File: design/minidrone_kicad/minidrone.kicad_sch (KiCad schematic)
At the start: 34 parts, among them J1 programming, J2 HM-13 Bluetooth, J3 BAT, J4 mpu6050, J5 FL Motor, J6 BL Motor, J7 FR Motor, J8 BR Motor, Q1 SI2302, Q2 SI2302, Q3 SI2302, Q4 SI2302, U1 stm32_BluePill

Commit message: fix(PCH/PCB): Programming pins and motor pins definition.
Correct the programming TX/RX connection.
Update the motor net-names due to the design changed.
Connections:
- net BL_PWM: now also Q3.1, R10.1, U1.32 (PA7); no longer Q2.1, R9.1, U1.31 (PA6)
- net BR_PWM: now also Q1.1, R8.1, U1.33 (PB0); no longer Q4.1, R11.1, U1.34 (PB1)
- net FL_PWM: now also Q4.1, R11.1, U1.34 (PB1); no longer Q1.1, R8.1, U1.33 (PB0)
- net FR_PWM: now also Q2.1, R9.1, U1.31 (PA6); no longer Q3.1, R10.1, U1.32 (PA7)
- net PRG_RX: now also J1.3 (Pin_3); no longer J1.4 (Pin_4)
- net PRG_TX: now also J1.4 (Pin_4); no longer J1.3 (Pin_3)
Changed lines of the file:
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@@
+		)
+	)
+	(label "FR_PWM"
+		(at 90.17 99.06 0)
+		(fields_autoplaced yes)
+		(effects
+			(font
+				(size 1.27 1.27)
+			)
+			(justify left bottom)
 		)
 	)
@@
 		)
 	)
-	(label "BR_PWM"
-		(at 90.17 91.44 0)
-		(fields_autoplaced yes)
-		(effects
-			(font
-				(size 1.27 1.27)
-			)
-			(justify left bottom)
-		)
-	)
-	(label "FL_PWM"
-		(at 140.97 99.06 0)
-		(fields_autoplaced yes)
-		(effects
-			(font
-				(size 1.27 1.27)
-			)
-			(justify left bottom)
-		)
-	)
 	(label "PRG_RX"
 		(at 41.91 96.52 0)
@@
 		)
 	)
-	(label "BL_PWM"
-		(at 140.97 142.24 0)
-		(fields_autoplaced yes)
-		(effects
-			(font
-				(size 1.27 1.27)
-			)
-			(justify left bottom)
-		)
-	)
 	(label "STAT_3"
 		(at 90.17 106.68 0)
@@
 		)
 	)
+	(label "PRG_TX"
+		(at 27.94 30.48 0)
+		(fields_autoplaced yes)
+		(effects
+			(font
+				(size 1.27 1.27)
+			)
+			(justify left bottom)
+		)
+	)
 	(label "MPU_SCL"
 		(at 40.64 116.84 0)
@@
 		)
 	)
-	(label "FR_PWM"
-		(at 90.17 96.52 0)
+	(label "BR_PWM"
+		(at 140.97 99.06 0)
 		(fields_autoplaced yes)
 		(effects
@@
 		)
 	)
+	(label "BR_PWM"
+		(at 90.17 93.98 0)
+		(fields_autoplaced yes)
+		(effects
+			(font
+				(size 1.27 1.27)
+			)
+			(justify left bottom)
+		)
+	)
 	(label "STAT_0"
 		(at 237.49 22.86 0)
@@
 		)
 	)
-	(label "FL_PWM"
-		(at 90.17 93.98 0)
-		(fields_autoplaced yes)
-		(effects
-			(font
-				(size 1.27 1.27)
-			)
-			(justify left bottom)
-		)
-	)
 	(label "BT_TX"
 		(at 90.17 86.36 0)
@@
 		)
 	)
+	(label "PRG_RX"
+		(at 27.94 27.94 0)
+		(fields_autoplaced yes)
+		(effects
+			(font
+				(size 1.27 1.27)
+			)
+			(justify left bottom)
+		)
+	)
+	(label "FL_PWM"
+		(at 90.17 91.44 0)
+		(fields_autoplaced yes)
+		(effects
+			(font
+				(size 1.27 1.27)
+			)
+			(justify left bottom)
+		)
+	)
 	(label "VBAT"
 		(at 161.29 33.02 0)
@@
 		)
 	)
-	(label "PRG_RX"
-		(at 27.94 30.48 0)
+	(label "BL_PWM"
+		(at 184.15 99.06 0)
 		(fields_autoplaced yes)
 		(effects
@@
 		)
 	)
+	(label "BL_PWM"
+		(at 90.17 96.52 0)
+		(fields_autoplaced yes)
+		(effects
+			(font
+				(size 1.27 1.27)
+			)
+			(justify left bottom)
+		)
+	)
 	(label "MPU_SCL"
 		(at 187.96 36.83 0)
@@
 		)
 	)
-	(label "BL_PWM"
-		(at 90.17 99.06 0)
-		(fields_autoplaced yes)
-		(effects
-			(font
-				(size 1.27 1.27)
-			)
-			(justify left bottom)
-		)
-	)
 	(label "BT_RX"
 		(at 90.17 88.9 0)
@@
 		)
 	)
+	(label "FR_PWM"
+		(at 140.97 142.24 0)
+		(fields_autoplaced yes)
+		(effects
+			(font
+				(size 1.27 1.27)
+			)
+			(justify left bottom)
+		)
+	)
 	(label "PRG_TX"
 		(at 41.91 99.06 0)
@@
 		)
 	)
-	(label "PRG_TX"
-		(at 27.94 27.94 0)
-		(fields_autoplaced yes)
-		(effects
-			(font
-				(size 1.27 1.27)
-			)
-			(justify left bottom)
-		)
-	)
-	(label "FR_PWM"
-		(at 184.15 99.06 0)
+	(label "FL_PWM"
+		(at 184.15 142.24 0)
 		(fields_autoplaced yes)
 		(effects
@@
 		(fields_autoplaced yes)
 		(effects
-			(font
-				(size 1.27 1.27)
-			)
-			(justify left bottom)
-		)
-	)
-	(label "BR_PWM"
-		(at 184.15 142.24 0)
-		(fields_autoplaced yes)
-		(effects

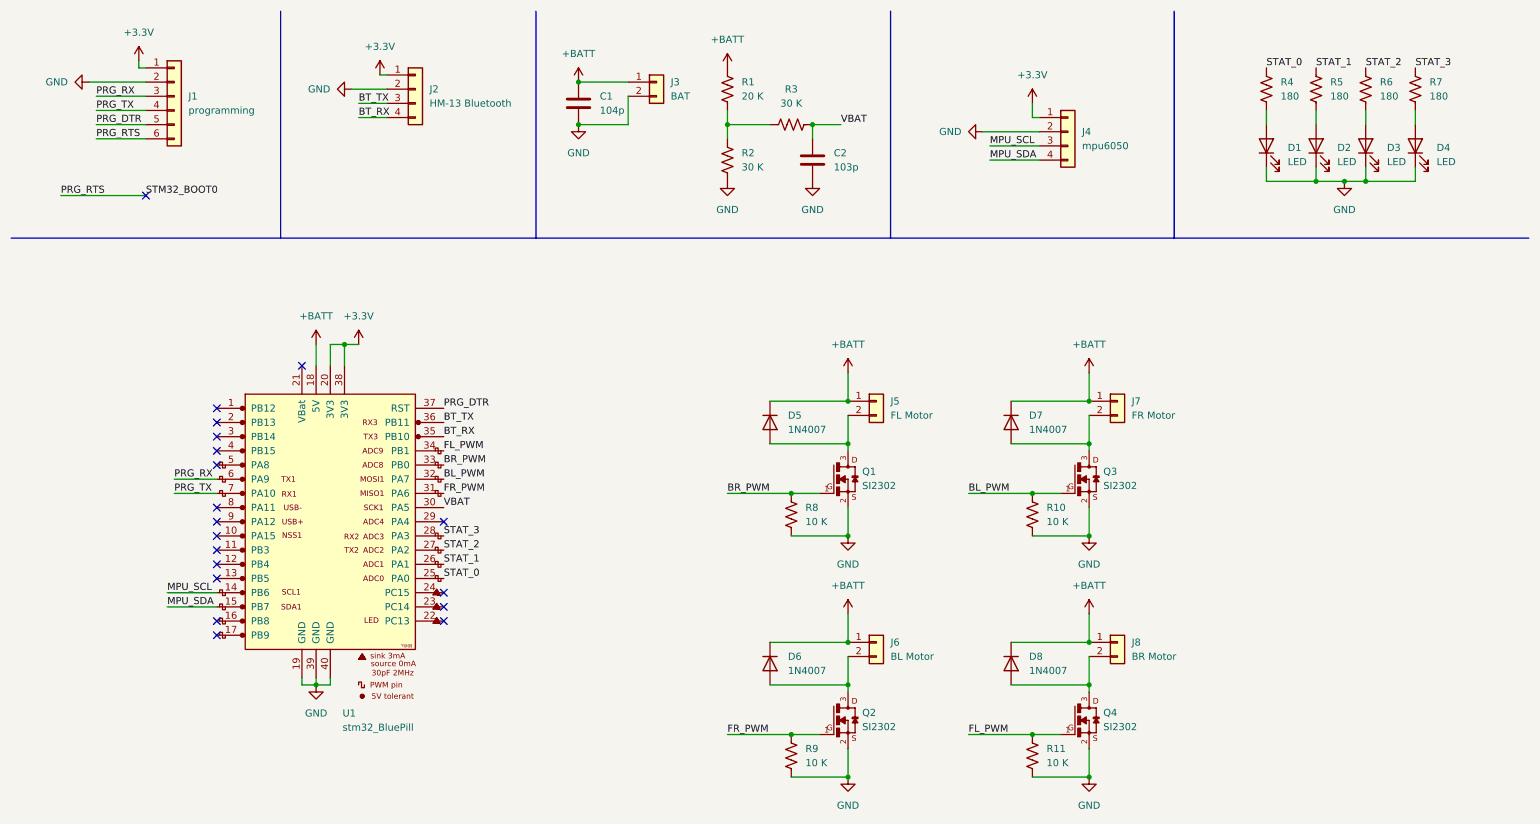
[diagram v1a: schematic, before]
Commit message: docs(SCH/PCB): Update the PCB design to v2.
The v1's handmade version is too heavy.
 - Remove the STM32 blue pill board.
 - Using the STM32F103CBT6 to make sure the ROM size enough.
 - Design the PCB as the drone's frame.
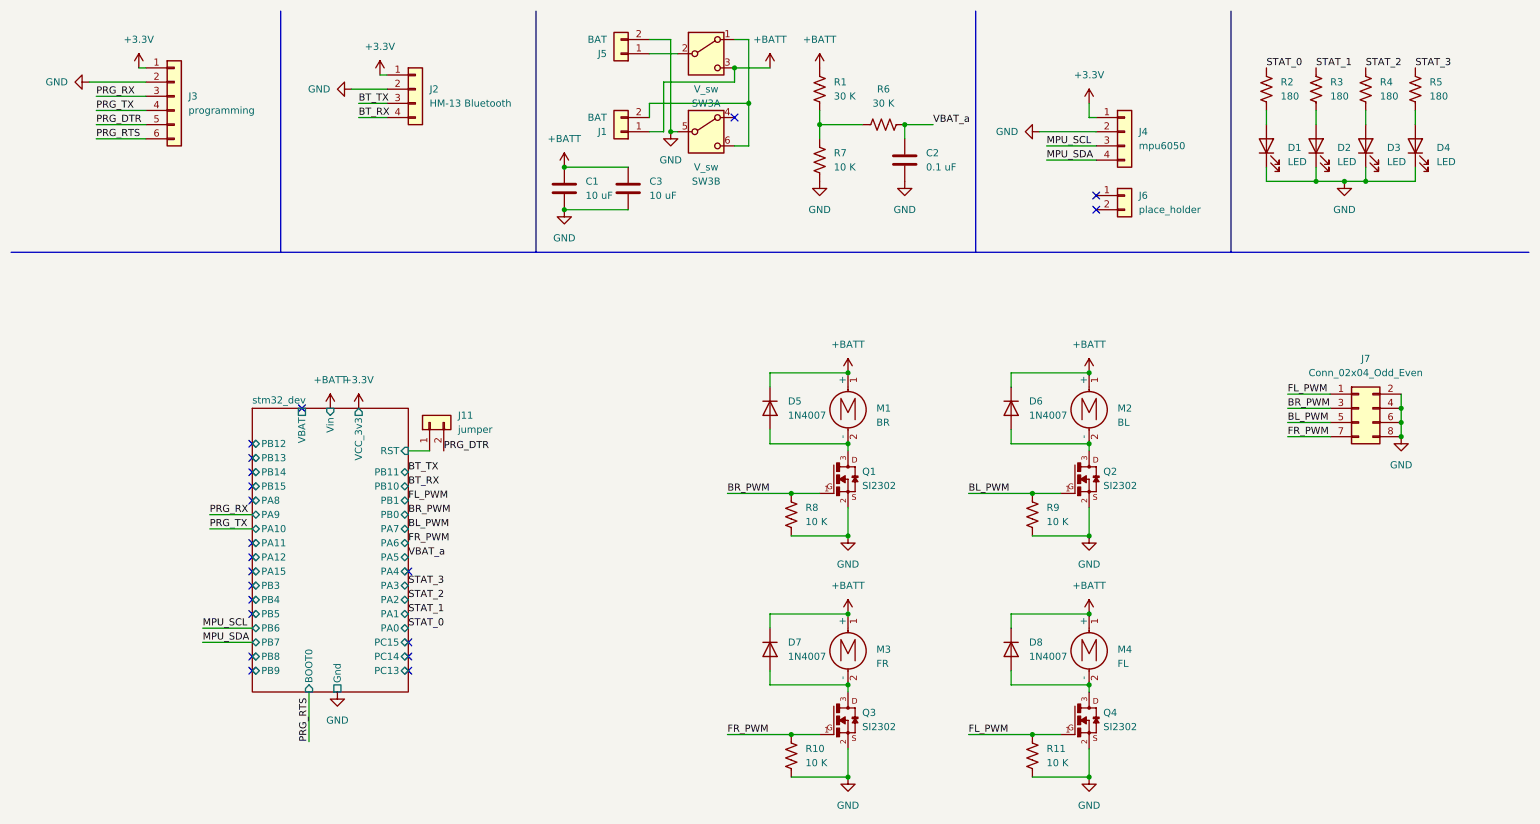
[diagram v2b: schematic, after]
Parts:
- removed J7: FR Motor, Connector_PinHeader_2.54mm:PinHeader_1x02_P2.54mm_Horizontal, symbol Connector_Generic:Conn_01x02
- removed J8: BR Motor, Connector_PinHeader_2.54mm:PinHeader_1x02_P2.54mm_Horizontal, symbol Connector_Generic:Conn_01x02
- removed U1: stm32_BluePill, STM32_module:stm32_BluePill_1, symbol STM32_module:stm32_BluePill
- added C3: 10 uF, Capacitor_SMD:C_1210_3225Metric_Pad1.33x2.70mm_HandSolder, symbol Device:C
- added J11: jumper, Connector_PinHeader_2.54mm:PinHeader_1x02_P2.54mm_Vertical, symbol Connector_Generic:Conn_01x02
- added J7: Conn_02x04_Odd_Even, Connector_PinHeader_2.54mm:PinHeader_2x04_P2.54mm_Vertical, symbol Connector_Generic:Conn_02x04_Odd_Even
- added M1: BR, Connector_PinHeader_2.54mm:PinHeader_1x02_P2.54mm_Horizontal, symbol Motor:Motor_DC
- added M2: BL, Connector_PinHeader_2.54mm:PinHeader_1x02_P2.54mm_Horizontal, symbol Motor:Motor_DC
- added M3: FR, Connector_PinHeader_2.54mm:PinHeader_1x02_P2.54mm_Horizontal, symbol Motor:Motor_DC
- added M4: FL, Connector_PinHeader_2.54mm:PinHeader_1x02_P2.54mm_Horizontal, symbol Motor:Motor_DC
- added SW3: V_sw, Button_Switch_THT:SW_CK_JS202011CQN_DPDT_Straight, symbol Switch:SW_DPDT_x2
- C1: value 104p -> 10 uF; footprint Capacitor_SMD:C_0603_1608Metric -> Capacitor_SMD:C_1210_3225Metric_Pad1.33x2.70mm_HandSolder
- C2: value 103p -> 0.1 uF; footprint Capacitor_SMD:C_0603_1608Metric -> Capacitor_SMD:C_0603_1608Metric_Pad1.08x0.95mm_HandSolder
- J1: renamed from J3; footprint Connector_JST:JST_PH_S2B-PH-K_1x02_P2.00mm_Horizontal -> Connector_PinHeader_2.54mm:PinHeader_1x02_P2.54mm_Horizontal
- J5: value FL Motor -> BAT
- J6: value BL Motor -> place_holder; footprint Connector_PinHeader_2.54mm:PinHeader_1x02_P2.54mm_Horizontal -> Connector_PinHeader_2.54mm:PinHeader_1x02_P2.54mm_Vertical
- R1: value 20 K -> 30 K
- R7: renamed from R2; value 30 K -> 10 K
- renumbered D7 to D6, D6 to D7, J1 to J3, Q3 to Q2, Q2 to Q3, R9 to R10, R4 to R2, R5 to R3, R6 to R4, R7 to R5, R3 to R6, R10 to R9
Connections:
- net +BATT: now also C3.1, M1.1 (+), M2.1 (+), M3.1 (+), M4.1 (+), SW3.3 (C); no longer J5.1 (Pin_1), J6.1 (Pin_1)
- net BL_PWM: now also J7.5 (Pin_5)
- net BR_PWM: now also J7.3 (Pin_3)
- net FL_PWM: now also J7.1 (Pin_1)
- net FR_PWM: now also J7.7 (Pin_7)
- net GND: now also J5.2 (Pin_2), C3.2, J7.2 (Pin_2), J7.4 (Pin_4), J7.6 (Pin_6), J7.8 (Pin_8), SW3.5 (B); no longer J1.2 (Pin_2)
- net PRG_DTR: now also J11.2 (Pin_2)
- net at D8.2 (A), Q4.3: now also M4.2 (-)
- net at D5.2 (A), Q1.3: now also M1.2 (-); no longer J5.2 (Pin_2)
- net at D6.2 (A), Q2.3: now also M2.2 (-)
- net at D7.2 (A), Q3.3: now also M3.2 (-); no longer J6.2 (Pin_2)
- net VBAT renamed VBAT_a
- new net: J1.2 (Pin_2), SW3.1 (A), SW3.6 (C)
- new net: J5.1 (Pin_1), SW3.2 (B)
- new net stm32_dev/RST: J11.1 (Pin_1)
- no-connect marks 19 -> 21
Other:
- added sheet stm32_dev (stm32_dev.kicad_sch)
- moved on the sheet: C1, C2, D5, D6, D7, D8, J1, J4, R1, R6, R7

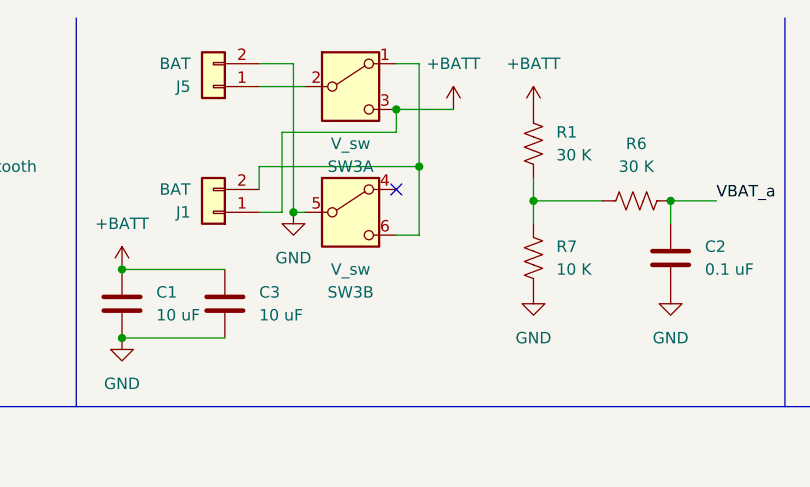
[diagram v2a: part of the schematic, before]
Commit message: fix(circuit): fix the battery series or parallel circuits
- Correct the invert connection on SW3
- Correct the silkscreen for voltage selection
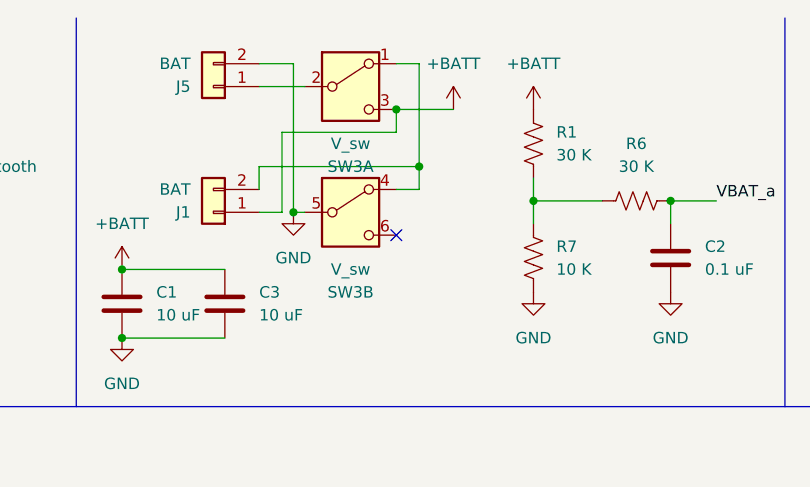
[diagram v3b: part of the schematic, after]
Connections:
- net at J1.2 (Pin_2), SW3.1 (A): now also SW3.4 (A); no longer SW3.6 (C)
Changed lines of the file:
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@@
+	)
+	(no_connect
+		(at 142.24 36.83)
 	)
 	(no_connect
@@
 	)
 	(no_connect
-		(at 142.24 31.75)
-	)
-	(no_connect
 		(at 83.82 130.81)
 	)
@@
 	(wire
 		(pts
+			(xy 144.78 31.75) (xy 142.24 31.75)
+		)
+		(stroke
+			(width 0)
+			(type default)
+		)
+	)
+	(wire
+		(pts
 			(xy 157.48 33.02) (xy 157.48 35.56)
 		)
@@
 	(wire
 		(pts
-			(xy 144.78 36.83) (xy 142.24 36.83)
-		)
-		(stroke
-			(width 0)
-			(type default)
-		)
-	)
-	(wire
-		(pts
 			(xy 129.54 25.4) (xy 142.24 25.4)
 		)
@@
 	(wire
 		(pts
+			(xy 144.78 29.21) (xy 144.78 31.75)
+		)
+		(stroke
+			(width 0)
+			(type default)
+		)
+	)
+	(wire
+		(pts
 			(xy 127 17.78) (xy 130.81 17.78)
 		)
@@
 		(pts
 			(xy 162.56 90.17) (xy 162.56 91.44)
-		)
-		(stroke
-			(width 0)
-			(type default)
-		)
-	)
-	(wire
-		(pts
-			(xy 144.78 29.21) (xy 144.78 36.83)
 		)
 		(stroke
@@
 	(label "MPU_SDA"
 		(at 198.12 39.37 0)
-		(fields_autoplaced yes)
 		(effects
 			(font
@@
 	(label "STAT_2"
 		(at 255.27 22.86 0)
-		(fields_autoplaced yes)
 		(effects
 			(font
@@
 	(label "STAT_2"
 		(at 83.82 118.11 0)
-		(fields_autoplaced yes)
 		(effects
 			(font
@@
 	(label "BT_RX"
 		(at 83.82 97.79 0)
-		(fields_autoplaced yes)
 		(effects
 			(font
@@
 	(label "PRG_RTS"
 		(at 27.94 35.56 0)
-		(fields_autoplaced yes)
 		(effects
 			(font
@@
 	(label "BR_PWM"
 		(at 241.3 83.82 0)
-		(fields_autoplaced yes)
 		(effects
 			(font
@@
 	(label "MPU_SDA"
 		(at 46.99 125.73 0)
-		(fields_autoplaced yes)
 		(effects
 			(font
@@
 	(label "STAT_3"
 		(at 83.82 115.57 0)
-		(fields_autoplaced yes)
 		(effects
 			(font
@@
 	(label "PRG_RTS"
 		(at 66.04 143.51 90)
-		(fields_autoplaced yes)
 		(effects
 			(font
@@
 	(label "PRG_TX"
 		(at 27.94 30.48 0)
-		(fields_autoplaced yes)
 		(effects
 			(font
@@
 	(label "BR_PWM"
 		(at 140.97 99.06 0)
-		(fields_autoplaced yes)
 		(effects
 			(font
@@
 	(label "BL_PWM"
 		(at 241.3 86.36 0)
-		(fields_autoplaced yes)
 		(effects
 			(font
@@
 	(label "VBAT_a"
 		(at 83.82 110.49 0)
-		(fields_autoplaced yes)
 		(effects
 			(font
@@
 	(label "STAT_1"
 		(at 246.38 22.86 0)
-		(fields_autoplaced yes)
 		(effects
 			(font
@@
 	(label "STAT_0"
 		(at 237.49 22.86 0)
-		(fields_autoplaced yes)
 		(effects
 			(font
@@
 	(label "PRG_TX"
 		(at 48.26 105.41 0)
-		(fields_autoplaced yes)
 		(effects
 			(font
@@
 	(label "BT_RX"
 		(at 74.93 31.75 0)
-		(fields_autoplaced yes)
 		(effects
 			(font
@@
 	(label "PRG_RX"
 		(at 27.94 27.94 0)
-		(fields_autoplaced yes)
 		(effects
 			(font
@@
 	(label "VBAT_a"
 		(at 177.8 33.02 0)
-		(fields_autoplaced yes)
 		(effects
 			(font
@@
 	(label "BL_PWM"
 		(at 184.15 99.06 0)
-		(fields_autoplaced yes)
 		(effects
 			(font
@@
 	(label "BL_PWM"
 		(at 83.82 105.41 0)
-		(fields_autoplaced yes)
 		(effects
 			(font
@@
 	(label "MPU_SCL"
 		(at 198.12 36.83 0)
-		(fields_autoplaced yes)
 		(effects
 			(font
@@
 	(label "MPU_SCL"
 		(at 46.99 123.19 0)
-		(fields_autoplaced yes)
 		(effects
 			(font
@@
 	(label "PRG_RX"
 		(at 48.26 102.87 0)
-		(fields_autoplaced yes)
 		(effects
 			(font
@@
 	(label "PRG_DTR"
 		(at 27.94 33.02 0)
-		(fields_autoplaced yes)
 		(effects
 			(font
@@
 	(label "STAT_1"
 		(at 83.82 120.65 0)
-		(fields_autoplaced yes)
 		(effects
 			(font
@@
 	(label "BR_PWM"
 		(at 83.82 102.87 0)
-		(fields_autoplaced yes)
 		(effects
 			(font
@@
 	(label "PRG_DTR"
 		(at 90.17 91.44 0)
-		(fields_autoplaced yes)
 		(effects
 			(font
@@
 	(label "FR_PWM"
 		(at 140.97 142.24 0)
-		(fields_autoplaced yes)
 		(effects
 			(font
@@
 	(label "STAT_3"
 		(at 264.16 22.86 0)
-		(fields_autoplaced yes)
 		(effects
 			(font
@@
 	(label "FL_PWM"
 		(at 184.15 142.24 0)
-		(fields_autoplaced yes)
 		(effects
 			(font
@@
 	(label "FR_PWM"
 		(at 83.82 107.95 0)
-		(fields_autoplaced yes)
 		(effects
 			(font
@@
 	(label "BT_TX"
 		(at 83.82 95.25 0)
-		(fields_autoplaced yes)
 		(effects
 			(font
@@
 	(label "FL_PWM"
 		(at 241.3 81.28 0)
-		(fields_autoplaced yes)
 		(effects
 			(font
@@
 	(label "BT_TX"
 		(at 74.93 29.21 0)
-		(fields_autoplaced yes)
 		(effects
 			(font
@@
 	(label "STAT_0"
 		(at 83.82 123.19 0)
-		(fields_autoplaced yes)
 		(effects
 			(font
@@
 	(label "FR_PWM"
 		(at 241.3 88.9 0)
-		(fields_autoplaced yes)
 		(effects
 			(font
@@
 	(label "FL_PWM"
 		(at 83.82 100.33 0)
-		(fields_autoplaced yes)
-		(effects
-			(font
+		(effects
+			(font

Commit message: fix(circuit): add mounting hole
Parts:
- added H1, H2, H3, H4: Pad, MountingHole:MountingHole_3.2mm_M3_ISO7380_Pad_TopBottom, symbol Mechanical:MountingHole_Pad
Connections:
- net GND: now also H1.1, H2.1, H3.1, H4.1
